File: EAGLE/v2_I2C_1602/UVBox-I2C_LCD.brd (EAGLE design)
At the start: 100 x 52.6 mm, 59 parts, among them IC1 ULN2003AD, IC2 PCF8574, Q1 16M, Q2 BC817, SW1 Start, SW2 Mode, SW3 Add, SW4 Sub, U1 7812DT, U2 7805DT

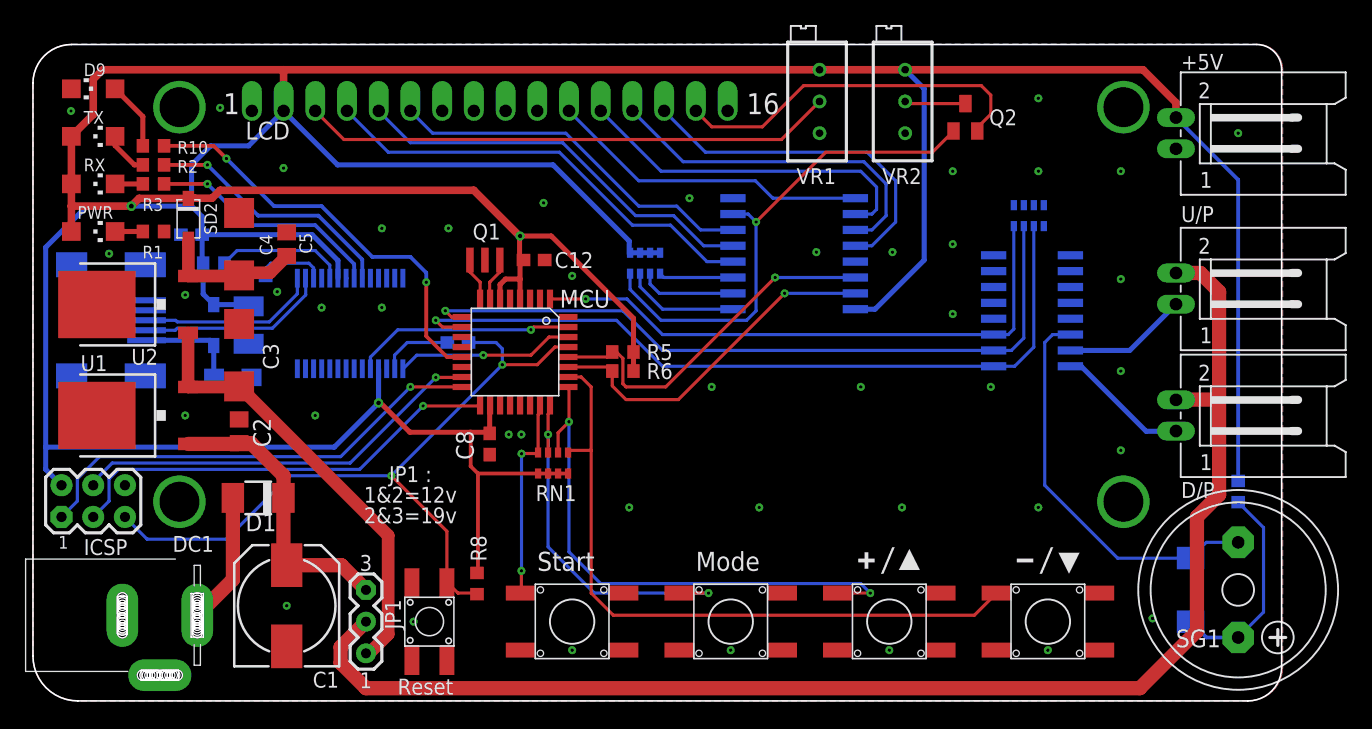
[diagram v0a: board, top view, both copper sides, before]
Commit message: 更換零件與微調線路
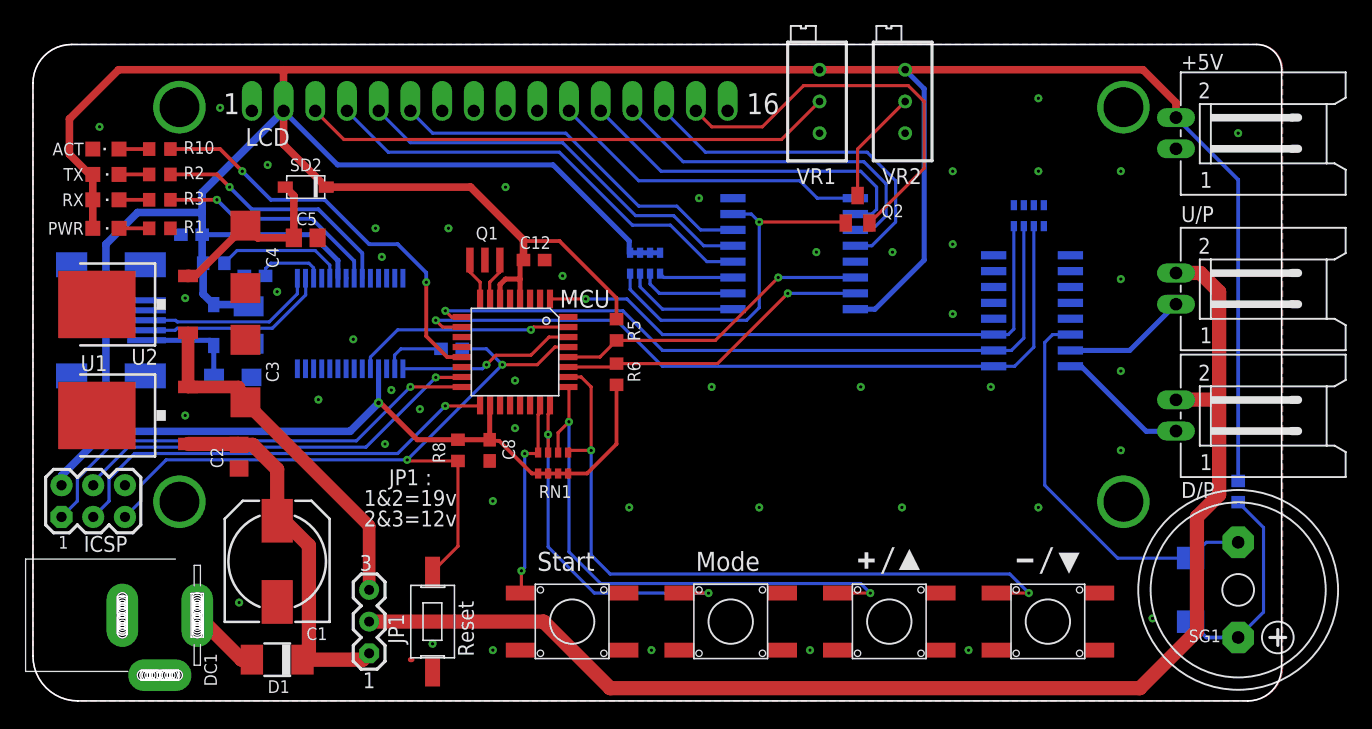
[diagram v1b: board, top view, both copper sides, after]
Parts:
- removed D9: Red, led:CHIPLED_1206
- added ACT: Red, led:CHIPLED_0805
- PWR, RX, TX: device led:CHIPLED_1206 -> led:CHIPLED_0805
- RESET: value SW-PUSH/4*4*3.8MM -> SW-PUSH/3*6*4.3MM; device 0_MyCustom:SW-4*4*3.8MM -> 0_MyCustom:SW-3*6*4.3MM
- moved D1 13.0 mm to (19.6, 3.30)
- moved Q2 11.4 mm to (66.0, 39.4)
- moved R8 10.8 mm to (34.0, 20.1)
- moved SD2 9.74 mm to (21.8, 41.1), turned to 0 degrees
- moved C1 3.64 mm to (19.6, 11.2)
- moved TX 3.21 mm to (5.84, 42.2)
- moved C2 2.03 mm to (16.5, 19.6), turned to 270 degrees
- moved R5 1.85 mm to (46.7, 29.7), turned to 270 degrees
- moved RX 1.63 mm to (5.84, 40.1)
- moved C5 1.61 mm to (21.8, 37.1), turned to 0 degrees
- moved R3 1.37 mm to (10.2, 40.1)
- moved C3 1.37 mm to (17.0, 26.4)
- moved C4 1.14 mm to (17.0, 35.6), turned to 270 degrees
- moved PWR 1.05 mm to (5.84, 37.8)
- moved R2 0.92 mm to (10.2, 42.2)
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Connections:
- net N$1 renamed VD
- net N$11 renamed D-
- net N$13 renamed RS
- net N$15 renamed D+
- net N$19 renamed !TXLED
- net N$20 renamed !RXLED
- net N$22 renamed PB1
- net N$23 renamed R/W
- net N$24 renamed E
- net N$5 renamed !RESET
- net N$6 renamed A2
- net N$61 renamed XTAL2
- net N$7 renamed A1
- net N$8 renamed A0
- net N$9 renamed XTAL1
- removed net N$21: D9.A, R10.2
- new net ACT_LED: ACT.A, R10.2
- net GND: now also ACT.C, RESET.1; no longer D9.C, RESET.3, RESET.4
- net RESET: no longer RESET.1
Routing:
- net +5V: track 392.0 -> 362.4 mm, vias 3 -> 1
- net IC2P3: track 40.8 -> 29.2 mm
- net 12V: track 35.6 -> 28.8 mm
- net 19V: track 23.4 -> 30.2 mm
- net N$21: track 5.49 -> 0.00 mm
- net PANEL_VCC: track 110.9 -> 105.9 mm
- net N$4: track 10.6 -> 5.85 mm
- net N$12: track 4.90 -> 9.11 mm
- net SCL: track 29.1 -> 25.6 mm
- net N$3: track 11.5 -> 14.9 mm
- net LCD_A: track 29.2 -> 32.3 mm
- net SDA: track 28.3 -> 25.4 mm
- net ACT_LED: track 0.00 -> 2.42 mm
- net KEY4: track 54.5 -> 56.5 mm, vias 0 -> 2
- net N$16: track 3.60 -> 2.42 mm
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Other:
- board text added: "JP1 : 1&2=19v 2&3=12v"
- board text removed: "JP1 : 1&2=12v 2&3=19v"
